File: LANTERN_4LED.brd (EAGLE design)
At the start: 26.9 x 26.9 mm, 7 parts

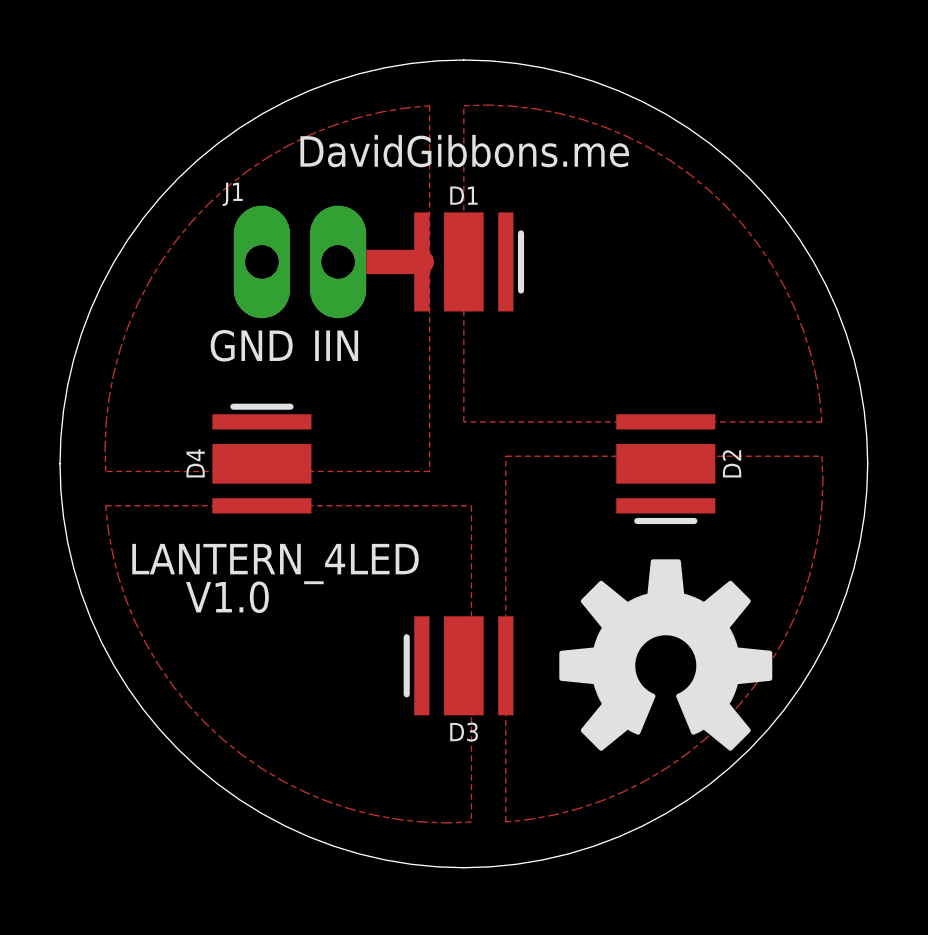
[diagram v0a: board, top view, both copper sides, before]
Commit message: Designed for 2 layer board
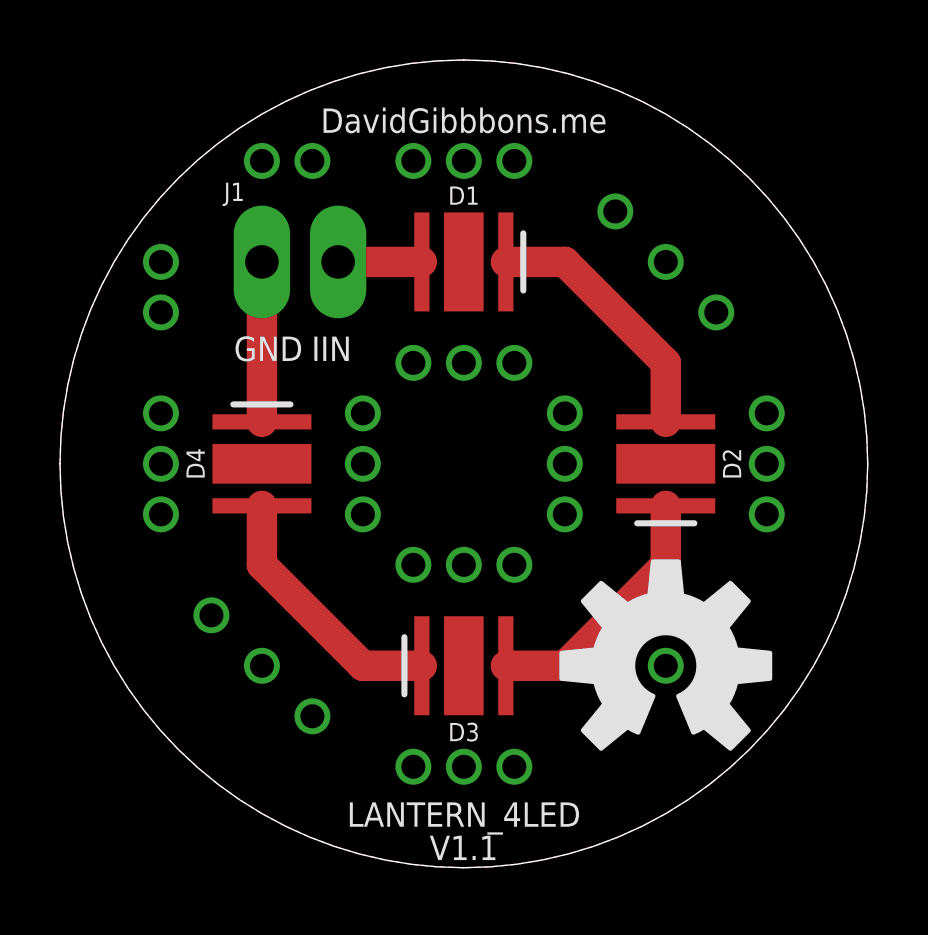
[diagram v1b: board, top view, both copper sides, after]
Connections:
- new net GND-ISO: D1.H, D2.H, D3.H, D4.H
- net GND: no longer D4.H
- net N$1: no longer D1.H
- net N$2: no longer D2.H
- net N$3: no longer D3.H
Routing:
- net N$1: track 0.00 -> 8.69 mm
- net N$2: track 0.00 -> 8.69 mm
- net N$3: track 0.00 -> 8.69 mm
- net GND: track 0.00 -> 5.33 mm
- added copper zone on layer 1, net GND-ISO
- added copper zone on layer 16, net GND-ISO
- removed copper zone on layer 1, net GND
- removed copper zone on layer 1, net N$1
- removed copper zone on layer 1, net N$2
- removed copper zone on layer 1, net N$3
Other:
- board text added: "DavidGibbbons.me"
- board text added: "V1.1"
- board text removed: "DavidGibbons.me"
- board text removed: "V1.0"

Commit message: Tied the heatsinks to ground.
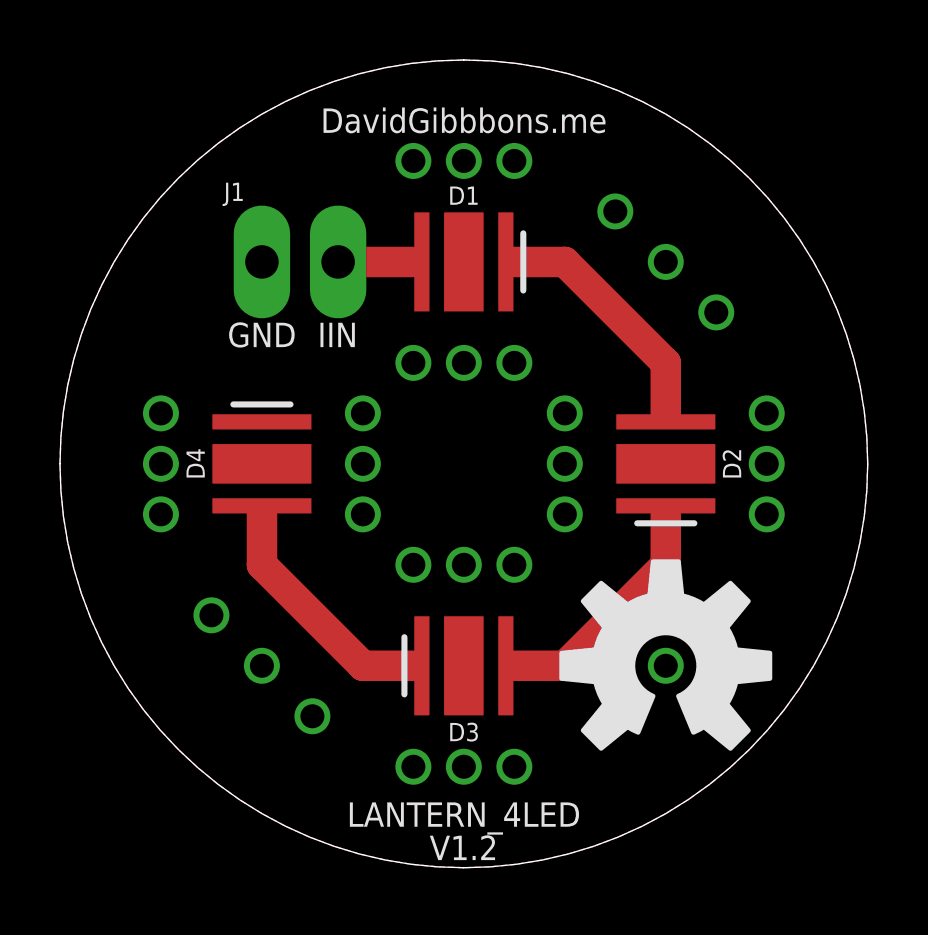
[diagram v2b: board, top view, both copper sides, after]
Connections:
- removed net GND-ISO: D1.H, D2.H, D3.H, D4.H
- net GND: now also D1.H, D2.H, D3.H, D4.H
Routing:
- net GND: track 5.33 -> 0.00 mm, vias 0 -> 33
- added copper zone on layer 1, net GND
- added copper zone on layer 16, net GND
- removed copper zone on layer 1, net GND-ISO
- removed copper zone on layer 16, net GND-ISO
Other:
- board text added: "V1.2"
- board text removed: "V1.1"
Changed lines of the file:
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@@
 <setting verticaltext="up"/>
 </settings>
-<grid distance="0.033125" unitdist="inch" unit="inch" style="lines" multiple="1" display="no" altdistance="0.033125" altunitdist="inch" altunit="inch"/>
+<grid distance="0.004140625" unitdist="inch" unit="inch" style="lines" multiple="1" display="no" altdistance="0.004140625" altunitdist="inch" altunit="inch"/>
 <layers>
 <layer number="1" name="Top" color="4" fill="1" visible="yes" active="yes"/>
@@
 <layer number="27" name="tValues" color="7" fill="1" visible="yes" active="yes"/>
 <layer number="28" name="bValues" color="7" fill="1" visible="yes" active="yes"/>
-<layer number="29" name="tStop" color="7" fill="3" visible="no" active="yes"/>
-<layer number="30" name="bStop" color="7" fill="6" visible="no" active="yes"/>
-<layer number="31" name="tCream" color="7" fill="4" visible="no" active="yes"/>
-<layer number="32" name="bCream" color="7" fill="5" visible="no" active="yes"/>
-<layer number="33" name="tFinish" color="6" fill="3" visible="no" active="yes"/>
-<layer number="34" name="bFinish" color="6" fill="6" visible="no" active="yes"/>
-<layer number="35" name="tGlue" color="7" fill="4" visible="no" active="yes"/>
-<layer number="36" name="bGlue" color="7" fill="5" visible="no" active="yes"/>
-<layer number="37" name="tTest" color="7" fill="1" visible="no" active="yes"/>
-<layer number="38" name="bTest" color="7" fill="1" visible="no" active="yes"/>
+<layer number="29" name="tStop" color="7" fill="3" visible="yes" active="yes"/>
+<layer number="30" name="bStop" color="7" fill="6" visible="yes" active="yes"/>
+<layer number="31" name="tCream" color="7" fill="4" visible="yes" active="yes"/>
+<layer number="32" name="bCream" color="7" fill="5" visible="yes" active="yes"/>
+<layer number="33" name="tFinish" color="6" fill="3" visible="yes" active="yes"/>
+<layer number="34" name="bFinish" color="6" fill="6" visible="yes" active="yes"/>
+<layer number="35" name="tGlue" color="7" fill="4" visible="yes" active="yes"/>
+<layer number="36" name="bGlue" color="7" fill="5" visible="yes" active="yes"/>
+<layer number="37" name="tTest" color="7" fill="1" visible="yes" active="yes"/>
+<layer number="38" name="bTest" color="7" fill="1" visible="yes" active="yes"/>
 <layer number="39" name="tKeepout" color="4" fill="11" visible="yes" active="yes"/>
 <layer number="40" name="bKeepout" color="1" fill="11" visible="yes" active="yes"/>
@@
 <layer number="43" name="vRestrict" color="2" fill="10" visible="yes" active="yes"/>
 <layer number="44" name="Drills" color="7" fill="1" visible="no" active="yes"/>
-<layer number="45" name="Holes" color="7" fill="1" visible="no" active="yes"/>
-<layer number="46" name="Milling" color="3" fill="1" visible="no" active="yes"/>
-<layer number="47" name="Measures" color="7" fill="1" visible="no" active="yes"/>
+<layer number="45" name="Holes" color="7" fill="1" visible="yes" active="yes"/>
+<layer number="46" name="Milling" color="3" fill="1" visible="yes" active="yes"/>
+<layer number="47" name="Measures" color="7" fill="1" visible="yes" active="yes"/>
 <layer number="48" name="Document" color="7" fill="1" visible="yes" active="yes"/>
 <layer number="49" name="Reference" color="7" fill="1" visible="yes" active="yes"/>
@@
 <layer number="112" name="tSilk" color="7" fill="1" visible="yes" active="yes"/>
 <layer number="113" name="IDFDebug" color="4" fill="1" visible="yes" active="yes"/>
-<layer number="114" name="Badge_Outline" color="7" fill="1" visible="no" active="yes"/>
-<layer number="115" name="ReferenceISLANDS" color="7" fill="1" visible="no" active="yes"/>
+<layer number="114" name="Badge_Outline" color="7" fill="1" visible="yes" active="yes"/>
+<layer number="115" name="ReferenceISLANDS" color="7" fill="1" visible="yes" active="yes"/>
 <layer number="116" name="Patch_BOT" color="9" fill="4" visible="yes" active="yes"/>
-<layer number="118" name="Rect_Pads" color="7" fill="1" visible="no" active="yes"/>
+<layer number="118" name="Rect_Pads" color="7" fill="1" visible="yes" active="yes"/>
 <layer number="121" name="_tsilk" color="7" fill="1" visible="yes" active="yes"/>
 <layer number="122" name="_bsilk" color="7" fill="1" visible="yes" active="yes"/>
@@
 <wire x1="26.924" y1="13.462" x2="13.462" y2="0" width="0" layer="20" curve="-90"/>
 <wire x1="13.462" y1="0" x2="0" y2="13.462" width="0" layer="20" curve="-90"/>
-<text x="5.794375" y="16.891" size="0.8128" layer="21" font="vector">GND</text>
-<text x="8.382" y="16.891" size="0.8128" layer="21" font="vector">IIN</text>
+<text x="6.731" y="17.353359375" size="0.8128" layer="21" font="vector" align="bottom-center">GND</text>
+<text x="9.255125" y="17.353359375" size="0.8128" layer="21" font="vector" align="bottom-center">IIN</text>
 <text x="13.462" y="24.495125" size="0.8128" layer="21" font="vector" align="bottom-center">DavidGibbbons.me</text>
 <text x="13.462" y="1.36525" size="0.8128" layer="21" font="vector" align="bottom-center">LANTERN_4LED</text>
-<text x="13.462" y="0.254" size="0.8128" layer="21" font="vector" align="bottom-center">V1.1</text>
+<text x="13.462" y="0.254" size="0.8128" layer="21" font="vector" align="bottom-center">V1.2</text>
 </plain>
 <attributes>
@@
 <contactref element="J1" pad="2"/>
 <contactref element="D1" pad="A"/>
-<wire x1="9.271" y1="20.193" x2="12.062" y2="20.193" width="1.016" layer="1"/>
+<wire x1="9.271" y1="20.193" x2="11.77925" y2="20.193" width="1.016" layer="1"/>
+<wire x1="11.77925" y1="20.193" x2="12.062" y2="20.193" width="0.254" layer="1"/>
 </signal>
 <signal name="GND">
 <contactref element="J1" pad="1"/>
 <contactref element="D4" pad="C"/>
-<wire x1="6.731" y1="14.86199375" x2="6.731" y2="20.193" width="1.016" layer="1"/>
-</signal>
-<signal name="N$1">
-<contactref element="D1" pad="C"/>
-<contactref element="D2" pad="A"/>
-<wire x1="14.86199375" y1="20.193" x2="16.8275" y2="20.193" width="1.016" layer="1"/>
-<wire x1="16.8275" y1="20.193" x2="20.193" y2="16.8275" width="1.016" layer="1"/>
-<wire x1="20.193" y1="16.8275" x2="20.193" y2="14.862" width="1.016" layer="1"/>
-</signal>
-<signal name="N$2">
-<contactref element="D2" pad="C"/>
-<contactref element="D3" pad="A"/>
-<wire x1="14.862" y1="6.731" x2="16.8275" y2="6.731" width="1.016" layer="1"/>
-<wire x1="16.8275" y1="6.731" x2="20.193" y2="10.0965" width="1.016" layer="1"/>
-<wire x1="20.193" y1="10.0965" x2="20.193" y2="12.06200625" width="1.016" layer="1"/>
-</signal>
-<signal name="N$3">
-<contactref element="D3" pad="C"/>
-<contactref element="D4" pad="A"/>
-<wire x1="6.731" y1="12.062" x2="6.731" y2="10.0965" width="1.016" layer="1"/>
-<wire x1="6.731" y1="10.0965" x2="10.0965" y2="6.731" width="1.016" layer="1"/>
-<wire x1="10.0965" y1="6.731" x2="12.06200625" y2="6.731" width="1.016" layer="1"/>
-</signal>
-<signal name="GND-ISO">
-<contactref element="D4" pad="H"/>
 <contactref element="D3" pad="H"/>
 <contactref element="D2" pad="H"/>
 <contactref element="D1" pad="H"/>
-<polygon width="1.3" layer="1">
+<contactref element="D4" pad="H"/>
+<polygon width="1.4224" layer="16">
 <vertex x="0" y="13.462" curve="-90"/>
 <vertex x="13.462" y="26.924" curve="-90"/>
@@
 <vertex x="13.462" y="0" curve="-90"/>
 </polygon>
-<polygon width="0.4064" layer="16">
+<polygon width="1.4224" layer="1">
 <vertex x="0" y="13.462" curve="-90"/>
 <vertex x="13.462" y="26.924" curve="-90"/>
@@
 <via x="20.193" y="20.193" extent="1-16" drill="0.8"/>
 <via x="20.193" y="6.731" extent="1-16" drill="0.8"/>
-<via x="3.3655" y="18.51025" extent="1-16" drill="0.8"/>
-<via x="8.41375" y="23.5585" extent="1-16" drill="0.8"/>
 <via x="10.0965" y="15.14475" extent="1-16" drill="0.8"/>
 <via x="10.0965" y="11.77925" extent="1-16" drill="0.8"/>
@@
 <via x="21.87575" y="8.41375" extent="1-16" drill="0.8"/>
 <via x="18.51025" y="5.04825" extent="1-16" drill="0.8"/>
-<via x="3.3655" y="20.193" extent="1-16" drill="0.8"/>
-<via x="6.731" y="23.5585" extent="1-16" drill="0.8"/>
+</signal>
+<signal name="N$1">
+<contactref element="D1" pad="C"/>
+<contactref element="D2" pad="A"/>
+<wire x1="14.86199375" y1="20.193" x2="15.14475" y2="20.193" width="0.254" layer="1"/>
+<wire x1="15.14475" y1="20.193" x2="16.8275" y2="20.193" width="1.016" layer="1"/>
+<wire x1="16.8275" y1="20.193" x2="20.193" y2="16.8275" width="1.016" layer="1"/>
+<wire x1="20.193" y1="16.8275" x2="20.193" y2="15.14475" width="1.016" layer="1"/>
+<wire x1="20.193" y1="15.14475" x2="20.193" y2="14.862" width="0.254" layer="1"/>
+</signal>
+<signal name="N$2">
+<contactref element="D2" pad="C"/>
+<contactref element="D3" pad="A"/>
+<wire x1="14.862" y1="6.731" x2="15.14475" y2="6.731" width="0.254" layer="1"/>
+<wire x1="15.14475" y1="6.731" x2="16.8275" y2="6.731" width="1.016" layer="1"/>
+<wire x1="16.8275" y1="6.731" x2="20.193" y2="10.0965" width="1.016" layer="1"/>
+<wire x1="20.193" y1="10.0965" x2="20.193" y2="11.77925" width="1.016" layer="1"/>
+<wire x1="20.193" y1="11.77925" x2="20.193" y2="12.06200625" width="0.254" layer="1"/>
+</signal>
+<signal name="N$3">
+<contactref element="D3" pad="C"/>
+<contactref element="D4" pad="A"/>
+<wire x1="6.731" y1="12.062" x2="6.731" y2="11.77925" width="0.254" layer="1"/>
+<wire x1="6.731" y1="11.77925" x2="6.731" y2="10.0965" width="1.016" layer="1"/>
+<wire x1="6.731" y1="10.0965" x2="10.0965" y2="6.731" width="1.016" layer="1"/>
+<wire x1="10.0965" y1="6.731" x2="11.77925" y2="6.731" width="1.016" layer="1"/>
+<wire x1="11.77925" y1="6.731" x2="12.06200625" y2="6.731" width="0.254" layer="1"/>
 </signal>
 </signals>
